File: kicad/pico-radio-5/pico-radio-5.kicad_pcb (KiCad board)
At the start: 2 copper layers, 41 parts, among them J1 HF Amplifier, J2 MW/SW antenna, J3 FM antenna, J4 SW antenna, Q1 PN2222A, Q2 PN2222A, SW1 Reset, U1 SI4732-A10-GS, U2 TFT_320x240, U3 KY-040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

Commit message: Refactor code structure for improved readability and maintainability
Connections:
- A1 pad 2: unconnected-(A1-GPIO1-Pad2) -> /LED
- A1 pad 22: unconnected-(A1-GPIO19-Pad22)_1 -> AUDIO_MUTE
- A1 pad 23: AUDIO_MUTE -> BUZZER
- A1 pad 24: TFT_LED -> unconnected-(A1-GPIO21-Pad24)_1
- A1 pad 25: BUZZER -> unconnected-(A1-GPIO22-Pad25)_1
- U2 pad 8: TFT_LED -> /LED
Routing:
- net GND: track 475.3 -> 527.3 mm
- net /LED: track 0.00 -> 15.3 mm
- net BUZZER: track 12.5 -> 16.6 mm
- net AUDIO_MUTE: track 74.0 -> 71.5 mm
- net /T_CS: track 40.4 -> 42.3 mm
- net +3.3V: track 165.6 -> 167.2 mm
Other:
- board outline added: 85 x 91.5 mm

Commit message: Refactor code structure for improved readability and maintainability
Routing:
- net /DC: track 27.0 -> 21.9 mm
- net +3.3V: track 167.2 -> 165.1 mm
- net GND: track 527.3 -> 526.5 mm
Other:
- board size 85 x 91.5 mm -> 86.5 x 91.5 mm

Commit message: Refactor code structure for improved readability and maintainability
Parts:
- added JP2: NYÁK átkötés, Resistor_THT:R_Axial_DIN0207_L6.3mm_D2.5mm_P7.62mm_Horizontal, F.Cu at (140.9, 97.0)
- moved C4 0.50 mm to (101.5, 81.0)
- moved C5 0.50 mm to (94.5, 81.0)
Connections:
- J1 pad 1: +Vbus -> Net-(J1-Pin_1)
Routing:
- net Net-(J1-Pin_1): track 0.00 -> 48.6 mm
- net +Vbus: track 89.2 -> 95.1 mm
- net Net-(J4-Pin_2): track 7.57 -> 9.62 mm
- net ROT_SW: track 34.7 -> 36.5 mm
- net AUDIO_R: track 37.0 -> 38.6 mm
- net AUDIO_L: track 24.8 -> 26.4 mm
- net +3.3V: track 165.1 -> 166.5 mm
- net AUDIO_MUTE: track 71.5 -> 70.6 mm
- net GND: track 526.5 -> 527.1 mm
- net Net-(U1-ROUT/DOUT): track 4.28 -> 3.78 mm
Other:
- board text added: "+"
- board text added: "1"
- board text added: "BT-Soft 2025"
- board text added: "FM"
- board text added: "MW"
- board text added: "SI4732-A10 - Pico Radio V5"
- board text added: "SW"

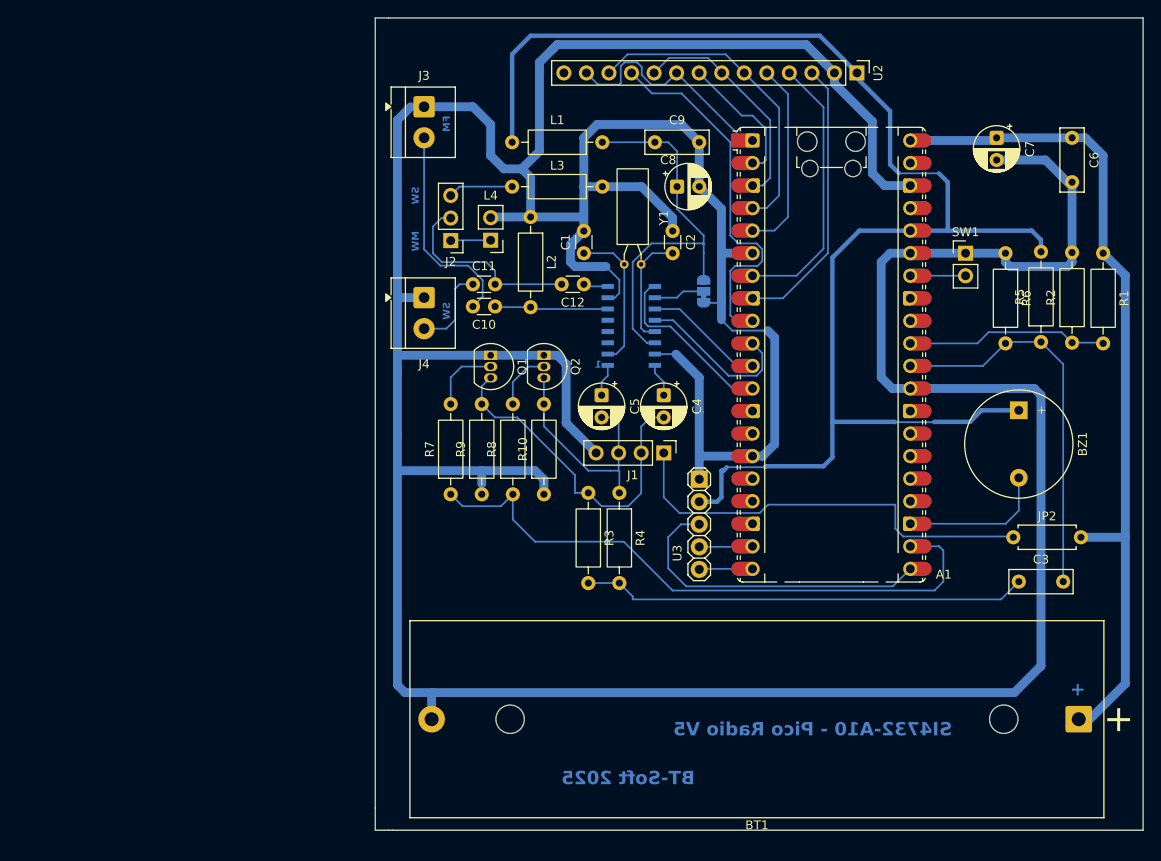
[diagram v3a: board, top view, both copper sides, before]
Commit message: Add lock file for pico-radio-5 schematic to prevent concurrent edits
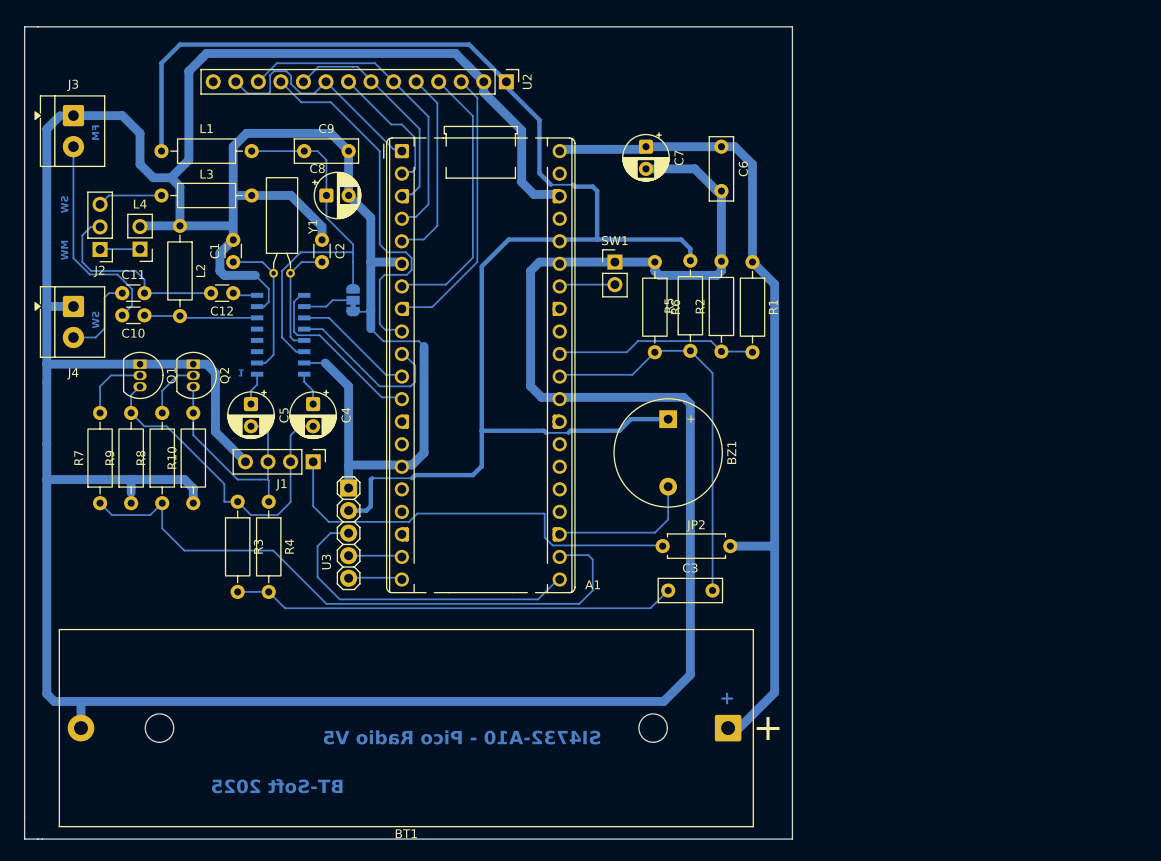
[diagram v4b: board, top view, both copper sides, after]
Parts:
- A1: footprint Module:RaspberryPi_Pico_Common_Unspecified -> Module:RaspberryPi_Pico_Common_THT-simple
- moved A1 53.5 mm to (72.0, 53.5)
- moved BT1 39.5 mm to (108.8, 118.5)
- moved BZ1 39.5 mm to (102.0, 83.7)
- moved C1 39.5 mm to (53.0, 66.0)
- moved C10 39.5 mm to (43.0, 72.0)
- moved C11 39.5 mm to (40.5, 69.5)
- moved C12 39.5 mm to (53.0, 69.5)
- moved C2 39.5 mm to (63.0, 63.5)
- moved C3 39.5 mm to (102.0, 103.0)
- moved C4 39.5 mm to (62.0, 82.0)
- moved C5 39.5 mm to (55.0, 82.0)
- moved C6 39.5 mm to (108.0, 53.0)
- moved C7 39.5 mm to (99.5, 53.0)
- moved C8 39.5 mm to (63.5, 58.5)
- moved C9 39.5 mm to (66.0, 53.5)
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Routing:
- net /Si_SDA: track 18.4 -> 19.3 mm

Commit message: Refactor code structure for improved readability and maintainability
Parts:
- removed BT1: BK-18650-PC2, Battery:BatteryHolder_MPD_BK-18650-PC2
- added J5: Batterry, Connector_PinHeader_2.54mm:PinHeader_1x02_P2.54mm_Vertical, F.Cu at (114.0, 92.5)
- added REF**: MountingHole_3.2mm_M3, MountingHole:MountingHole_3.2mm_M3, F.Cu at (32.2, 43.8)
- added REF**: MountingHole_3.2mm_M3, MountingHole:MountingHole_3.2mm_M3, F.Cu at (112.5, 43.8)
- added REF**: MountingHole_3.2mm_M3, MountingHole:MountingHole_3.2mm_M3, F.Cu at (32.2, 103.8)
- added REF**: MountingHole_3.2mm_M3, MountingHole:MountingHole_3.2mm_M3, F.Cu at (112.5, 103.8)
- moved C3 1.82 mm to (101.5, 101.2)
- moved JP1 0.75 mm to (65.8, 70.3)
- moved J3 0.50 mm to (35.0, 50.0)
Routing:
- net +Vbus: track 95.1 -> 71.1 mm
- net GND: track 527.1 -> 514.6 mm
- net Net-(C3-Pad1): track 50.1 -> 52.1 mm
- net AD_FFT_AUDIO: track 43.9 -> 41.9 mm
- net Net-(JP1-B): track 44.1 -> 43.0 mm
- net Net-(JP1-C): track 5.80 -> 5.05 mm
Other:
- board size 86.5 x 91.5 mm -> 87.2 x 67 mm
- board text added: "Pico Radio V5 SI4732-A10-GS"
- board text removed: "SI4732-A10 - Pico Radio V5"

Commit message: Refactor code structure for improved readability and maintainability
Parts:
- added Q3: PN2222A, Package_TO_SOT_THT:TO-92_Inline, F.Cu at (101.0, 94.8)
- added R11: 4.7k, Resistor_THT:R_Axial_DIN0207_L6.3mm_D2.5mm_P10.16mm_Horizontal, F.Cu at (94.2, 96.5)
- JP2: footprint Resistor_THT:R_Axial_DIN0207_L6.3mm_D2.5mm_P7.62mm_Horizontal -> Resistor_THT:R_Axial_DIN0207_L6.3mm_D2.5mm_P10.16mm_Horizontal
- moved U2 10.1 mm to (73.8, 44.2)
- moved JP2 3.80 mm to (97.6, 98.2)
- moved BZ1 3.35 mm to (98.7, 83.8), turned to 0 degrees
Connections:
- BZ1 pad 2: BUZZER -> Net-(BZ1--)
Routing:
- net GND: track 514.6 -> 541.8 mm
- net /SDO: track 26.7 -> 42.7 mm
- net /SCK: track 25.6 -> 41.1 mm
- net AUDIO_MUTE: track 71.0 -> 86.5 mm
- net /LED: track 15.3 -> 30.5 mm
- net /SDI: track 36.0 -> 50.5 mm
- net /T_CS: track 42.3 -> 56.3 mm
- net Net-(Q3-B): track 0.00 -> 12.3 mm
- net Net-(BZ1--): track 0.00 -> 12.3 mm
- net BUZZER: track 16.6 -> 4.57 mm
- net /DC: track 21.9 -> 33.0 mm
- net +3.3V: track 166.7 -> 176.5 mm
- net /RST: track 30.7 -> 37.0 mm
- net /CS: track 31.7 -> 37.6 mm
- net Net-(J1-Pin_1): track 48.6 -> 54.3 mm
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
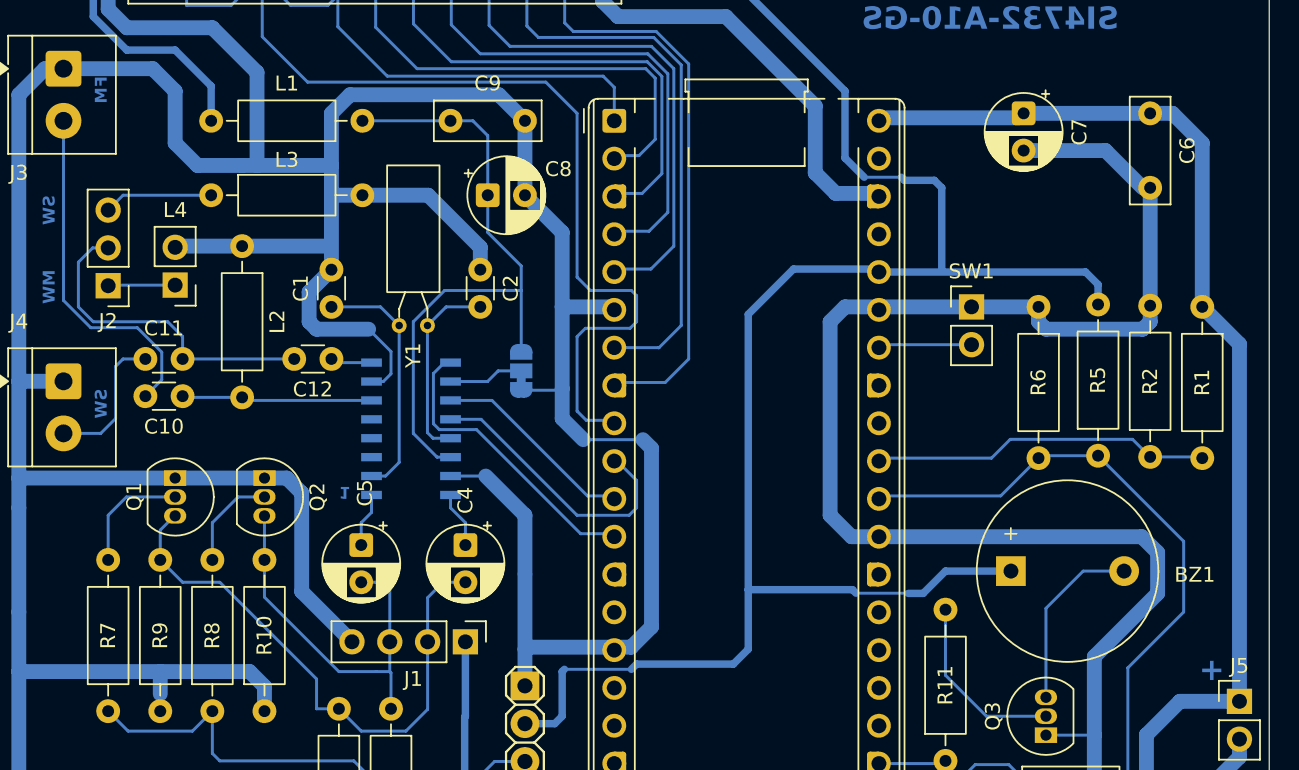
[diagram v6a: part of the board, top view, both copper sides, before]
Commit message: Add initial bill of materials for pico-radio project
- Created a new CSV file containing the bill of materials (BOM) for the pico-radio project.
- Included components such as transistors, capacitors, resistors, connectors, and other essential parts.
- Specified designators, footprints, quantities, and designations for each component.
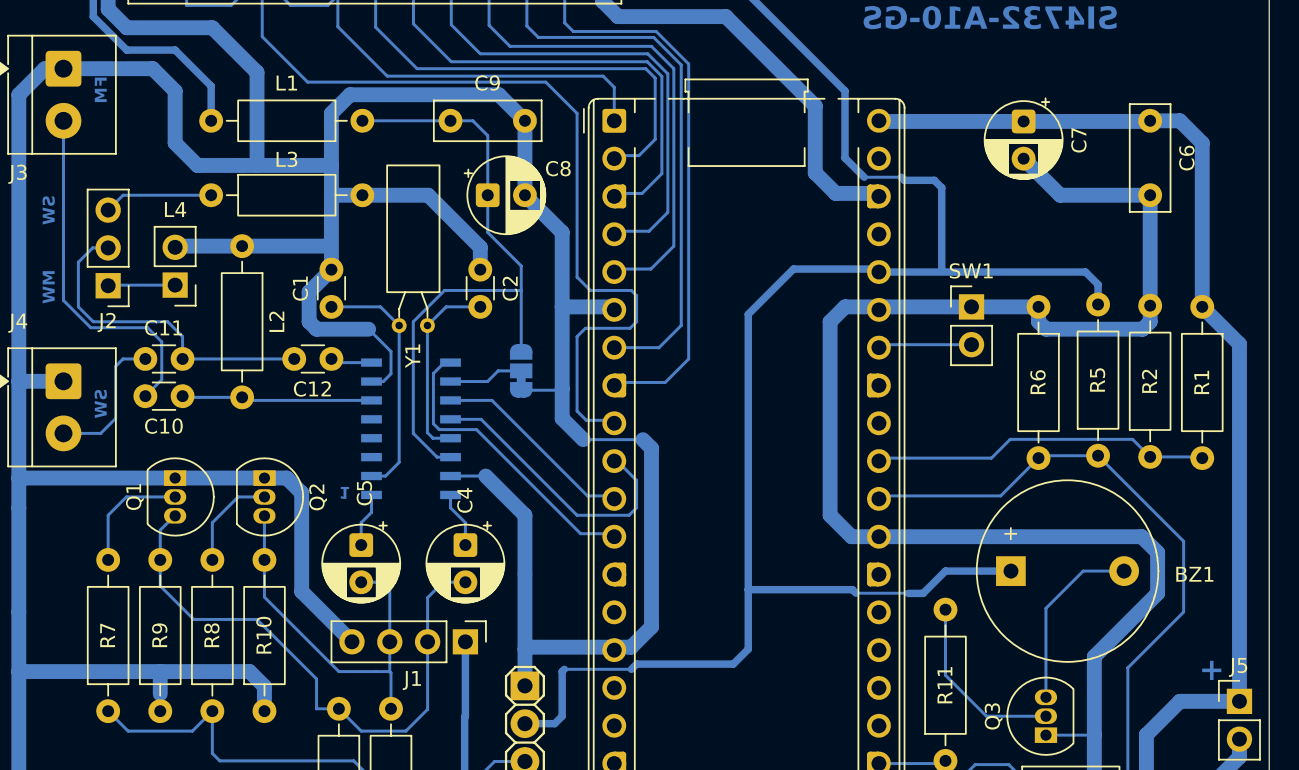
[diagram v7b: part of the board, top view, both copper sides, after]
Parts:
- moved C7 0.54 mm to (99.5, 53.5)
- moved C6 0.50 mm to (108.0, 53.5)
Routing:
- net AUDIO_R: track 38.6 -> 39.6 mm
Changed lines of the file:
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@@
 		(tenting front back)
 		(pcbplotparams
-			(layerselection 0x00000000_00000000_55555555_5755f5ff)
+			(layerselection 0x00000000_00000000_55555555_575555fc)
 			(plot_on_all_layers_selection 0x00000000_00000000_00000000_00000000)
 			(disableapertmacros no)
@@
 			(outputformat 1)
 			(mirror no)
-			(drillshape 1)
+			(drillshape 0)
 			(scaleselection 1)
-			(outputdirectory "")
+			(outputdirectory "../nyák rendelés/")
 		)
 	)
@@
 	(footprint "Capacitor_THT:CP_Radial_D5.0mm_P2.50mm"
 		(layer "F.Cu")
-		(at 99.5 53 -90)
+		(at 99.5 53.544888 -90)
 		(descr "CP, Radial series, Radial, pin pitch=2.50mm, diameter=5mm, height=7mm, Electrolytic Capacitor")
 		(tags "CP Radial series Radial pin pitch 2.50mm diameter 5mm height 7mm Electrolytic Capacitor")
@@
 	(footprint "Capacitor_THT:C_Disc_D7.0mm_W2.5mm_P5.00mm"
 		(layer "F.Cu")
-		(at 108 53 -90)
+		(at 108 53.5 -90)
 		(descr "C, Disc series, Radial, pin pitch=5.00mm, diameter*width=7*2.5mm^2, Capacitor, http://cdn-reichelt.de/documents/datenblatt/B300/DS_KERKO_TC.pdf")
 		(tags "C Disc series Radial pin pitch 5.00mm diameter 7mm width 2.5mm Capacitor")
@@
 	)
 	(segment
-		(start 105 55.5)
-		(end 99.5 55.5)
-		(width 1)
-		(layer "B.Cu")
-		(net 3)
-	)
-	(segment
 		(start 86.88 58.38)
 		(end 85.5 57)
@@
 	)
 	(segment
-		(start 107.5 58)
-		(end 105 55.5)
+		(start 101.955112 58.5)
+		(end 99.5 56.044888)
 		(width 1)
 		(layer "B.Cu")
@@
 	)
 	(segment
+		(start 108 65.92)
+		(end 108 58.5)
+		(width 1)
+		(layer "B.Cu")
+		(net 3)
+	)
+	(segment
 		(start 74.5 87.5)
 		(end 74.5 75.5)
@@
 	)
 	(segment
+		(start 108 58.5)
+		(end 101.955112 58.5)
+		(width 1)
+		(layer "B.Cu")
+		(net 3)
+	)
+	(segment
 		(start 68.5 66)
 		(end 68.5 71.5)
@@
 	)
 	(segment
-		(start 108 65.92)
-		(end 108 58)
-		(width 1)
-		(layer "B.Cu")
-		(net 3)
-	)
-	(segment
 		(start 32 79.5)
 		(end 32 77.5)
@@
 	)
 	(segment
+		(start 99.5 53.544888)
+		(end 107.955112 53.544888)
+		(width 1)
+		(layer "B.Cu")
+		(net 18)
+	)
+	(segment
 		(start 107.75 94.75)
 		(end 107.75 98.25)
@@
 	)
 	(segment
-		(start 114 68.5)
-		(end 111.5 66)
+		(start 108 53.5)
+		(end 110 53.5)
 		(width 1)
 		(layer "B.Cu")
@@
 	(segment
 		(start 114 68.5)
-		(end 114 92.5)
+		(end 111.5 66)
 		(width 1)
 		(layer "B.Cu")
@@
 	)
 	(segment
-		(start 114 92.5)
-		(end 110 92.5)
+		(start 99.5 53.544888)
+		(end 89.824888 53.544888)
 		(width 1)
 		(layer "B.Cu")
@@
 	)
 	(segment
-		(start 110 92.5)
-		(end 107.75 94.75)
+		(start 114 68.5)
+		(end 114 92.5)
 		(width 1)
 		(layer "B.Cu")
@@
 	)
 	(segment
-		(start 108 53)
-		(end 99.5 53)
+		(start 114 92.5)
+		(end 110 92.5)
 		(width 1)
 		(layer "B.Cu")
@@
 	)
 	(segment
-		(start 111.5 55)
-		(end 109.5 53)
+		(start 110 92.5)
+		(end 107.75 94.75)
 		(width 1)
 		(layer "B.Cu")
@@
 	)
 	(segment
-		(start 89.78 53.3)
-		(end 99.2 53.3)
-		(width 1)
+		(start 89.824888 53.544888)
+		(end 89.78 53.5)
+		(width 0.2)
 		(layer "B.Cu")
 		(net 18)
 	)
 	(segment
-		(start 109.5 53)
-		(end 108 53)
-		(width 1)
+		(start 107.955112 53.544888)
+		(end 108 53.5)
+		(width 0.2)
 		(layer "B.Cu")
 		(net 18)
@@
 	)
 	(segment
-		(start 99.2 53.3)
-		(end 99.5 53)
-		(width 0.2)
+		(start 110 53.5)
+		(end 111.5 55)
+		(width 1)
 		(layer "B.Cu")
 		(net 18)
@@
 	)
 	(segment
-		(start 45.5 84.5)
-		(end 52 91)
-		(width 0.2)
-		(layer "B.Cu")
-		(net 33)
-	)
-	(segment
 		(start 42.46 80.04)
 		(end 41.5 81)
@@
 	)
 	(segment
+		(start 52 91)
+		(end 52 93)
+		(width 0.2)
+		(layer "B.Cu")
+		(net 33)
+	)
+	(segment
 		(start 59.46 93.04)
 		(end 59.46 88.5)
@@
 	)
 	(segment
-		(start 42.5 80.04)
-		(end 42.46 80.04)
+		(start 41.5 83)
+		(end 41.5 84.75)
 		(width 0.2)
 		(layer "B.Cu")
@@
 	)
 	(segment
-		(start 41.5 83)
-		(end 43 84.5)
+		(start 42.5 80.04)
+		(end 42.46 80.04)
 		(width 0.2)
 		(layer "B.Cu")
@@
 	)
 	(segment
-		(start 52 91)
-		(end 52 93)
+		(start 61.5 84.5)
+		(end 60.5 84.5)
 		(width 0.2)
 		(layer "B.Cu")
@@
 	)
 	(segment
-		(start 61.5 84.5)
-		(end 60.5 84.5)
+		(start 53.5 93)
+		(end 55 94.5)
 		(width 0.2)
 		(layer "B.Cu")
@@
 	)
 	(segment
-		(start 53.5 93)
-		(end 55 94.5)
+		(start 48 87)
+		(end 52 91)
 		(width 0.2)
 		(layer "B.Cu")
@@
 	)
 	(segment
-		(start 62 85)
-		(end 61.5 84.5)
+		(start 43.75 87)
+		(end 48 87)
 		(width 0.2)
 		(layer "B.Cu")
@@
 	)
 	(segment
-		(start 55 94.5)
-		(end 58 94.5)
+		(start 41.5 84.75)
+		(end 43.75 87)
 		(width 0.2)
 		(layer "B.Cu")
@@
 	)
 	(segment
-		(start 43 84.5)
-		(end 45.5 84.5)
+		(start 62 85)
+		(end 61.5 84.5)
+		(width 0.2)
+		(layer "B.Cu")
+		(net 33)
+	)
+	(segment
+		(start 55 94.5)
+		(end 58 94.5)
 		(width 0.2)
 		(layer "B.Cu")
@@
 	)
 	(segment
-		(start 41.601 70.899)
-		(end 41.601 69.04395)
+		(start 40.651 67.401)
+		(end 36.8339 67.401)
 		(width 0.2)
 		(layer "B.Cu")
@@
 	)
 	(segment
-		(start 41.601 69.04395)
-		(end 39.95805 67.401)
+		(start 41.601 70.899)
+		(end 41.601 68.351)
 		(width 0.2)
 		(layer "B.Cu")
@@
 	)
 	(segment
-		(start 40.5 72)
-		(end 41.601 70.899)
+		(start 35 65.5671)
+		(end 35 53.5)
 		(width 0.2)
 		(layer "B.Cu")
@@
 	)
 	(segment
-		(start 39.95805 67.401)
-		(end 36.8339 67.401)
+		(start 40.5 72)
+		(end 41.601 70.899)
 		(width 0.2)
 		(layer "B.Cu")
@@
 	)
 	(segment
-		(start 35 65.5671)
-		(end 35 53.5)
+		(start 41.601 68.351)
+		(end 40.651 67.401)
 		(width 0.2)
 		(layer "B.Cu")

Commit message: Refactor code structure for improved readability and maintainability
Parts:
- added JP3: TFT SDO, Jumper:SolderJumper-2_P1.3mm_Open_RoundedPad1.0x1.5mm, B.Cu at (53.5, 48.1)
- L1: value 47uH -> 220uH
- L2: value 270uH -> 220uH
- R1: value 200k -> 10k
- R2: value 100k -> 15k
- moved BZ1 9.90 mm to (108.5, 83.8), turned to 180 degrees
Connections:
- BZ1 pad 1: +3.3V -> +Vbus
- U2 pad 9: /SDO -> Net-(JP3-A)
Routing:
- net GND: track 541.7 -> 561.0 mm
- net +3.3V: track 176.5 -> 159.5 mm
- net +Vbus: track 71.6 -> 77.0 mm
- net Net-(BZ1--): track 12.3 -> 8.50 mm
- net Net-(JP3-A): track 0.00 -> 3.23 mm
- net AD_FFT_AUDIO: track 45.5 -> 42.4 mm
- net /SDO: track 42.7 -> 40.2 mm
- net AUDIO_MUTE: track 86.5 -> 88.1 mm
- net /Si_SDA: track 19.3 -> 20.3 mm
